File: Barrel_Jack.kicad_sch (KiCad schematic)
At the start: 26 parts, among them J10 Barrel_Jack, J11 Barrel_Jack, J12 Barrel_Jack, J13 Barrel_Jack, J14 Barrel_Jack, J6 Barrel_Jack, J8 Barrel_Jack, J9 Barrel_Jack, U12 PCF8574ATS, U19 34.81-9024, U20 34.81-9024, U21 34.81-9024, U22 34.81-9024, U23 34.81-9024, U24 34.81-9024, U25 34.81-9024, U26 34.81-9024

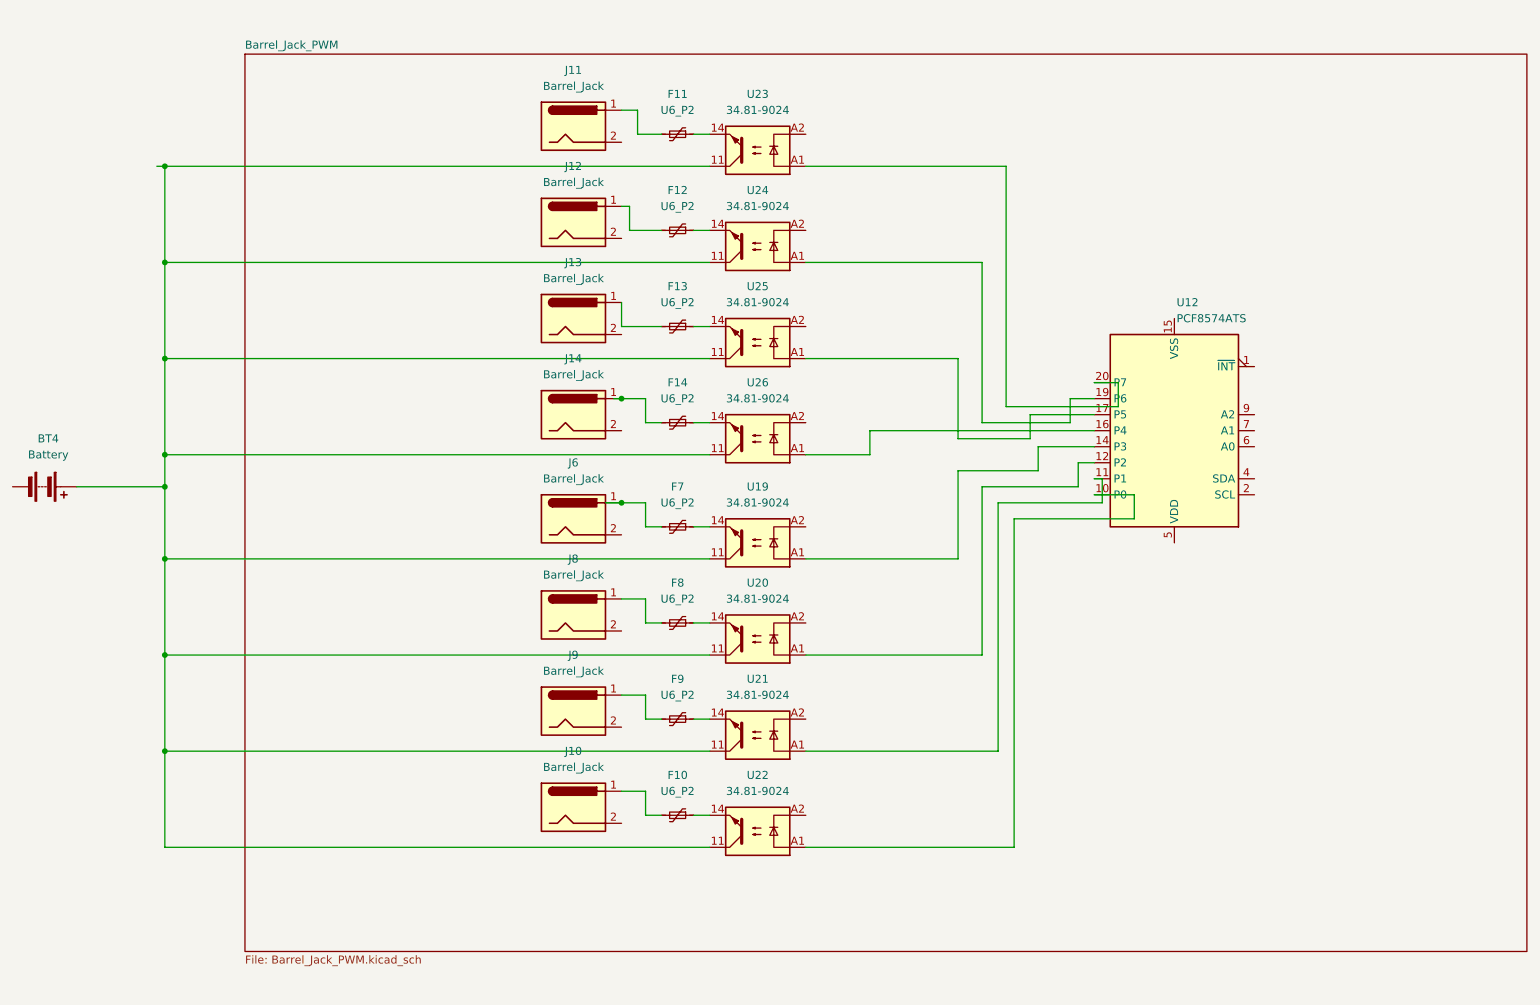
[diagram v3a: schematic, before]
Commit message: placeholders for ethernet and relay inputs
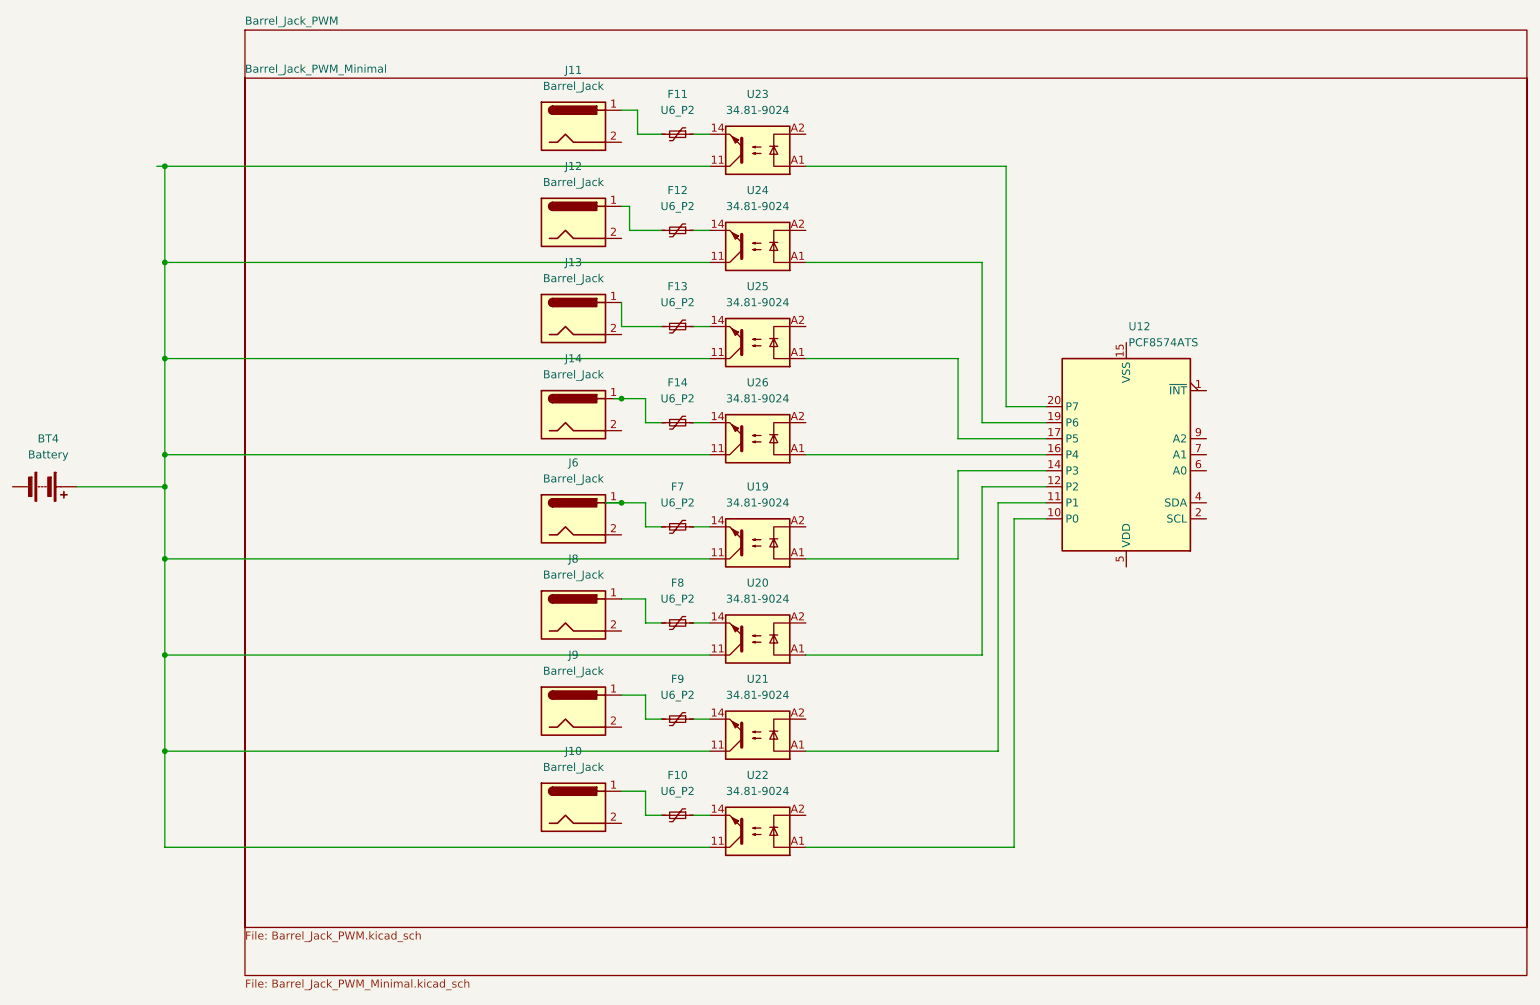
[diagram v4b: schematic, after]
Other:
- added sheet Barrel_Jack_PWM_Minimal (Barrel_Jack_PWM_Minimal.kicad_sch)
- moved on the sheet: U12
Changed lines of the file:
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@@
-    (stroke (width 0) (type default))
-  )
-  (wire (pts (xy 214.63 93.98) (xy 195.58 93.98))
-    (stroke (width 0) (type default))
-  )
-  (wire (pts (xy 205.74 88.9) (xy 205.74 85.09))
-    (stroke (width 0) (type default))
-  )
-  (wire (pts (xy 212.09 76.2) (xy 212.09 72.39))
     (stroke (width 0) (type default))
   )
@@
     (stroke (width 0) (type default))
   )
-  (wire (pts (xy 172.72 83.82) (xy 172.72 80.01))
-    (stroke (width 0) (type default))
-  )
   (wire (pts (xy 139.7 78.74) (xy 137.16 78.74))
     (stroke (width 0) (type default))
@@
     (stroke (width 0) (type default))
   )
-  (wire (pts (xy 209.55 87.63) (xy 208.28 87.63))
-    (stroke (width 0) (type default))
-  )
-  (wire (pts (xy 209.55 91.44) (xy 209.55 87.63))
-    (stroke (width 0) (type default))
-  )
   (wire (pts (xy 134.62 44.45) (xy 133.35 44.45))
     (stroke (width 0) (type default))
@@
     (stroke (width 0) (type default))
   )
-  (wire (pts (xy 204.47 78.74) (xy 190.5 78.74))
+  (wire (pts (xy 190.5 78.74) (xy 200.66 78.74))
     (stroke (width 0) (type default))
   )
@@
     (stroke (width 0) (type default))
   )
-  (wire (pts (xy 190.5 88.9) (xy 205.74 88.9))
-    (stroke (width 0) (type default))
-  )
-  (wire (pts (xy 204.47 74.93) (xy 208.28 74.93))
+  (wire (pts (xy 190.5 88.9) (xy 200.66 88.9))
     (stroke (width 0) (type default))
   )
@@
     (stroke (width 0) (type default))
   )
-  (wire (pts (xy 212.09 72.39) (xy 208.28 72.39))
-    (stroke (width 0) (type default))
-  )
-  (wire (pts (xy 199.39 82.55) (xy 208.28 82.55))
-    (stroke (width 0) (type default))
-  )
-  (wire (pts (xy 198.12 81.28) (xy 186.69 81.28))
+  (wire (pts (xy 194.31 76.2) (xy 200.66 76.2))
+    (stroke (width 0) (type default))
+  )
+  (wire (pts (xy 186.69 81.28) (xy 200.66 81.28))
     (stroke (width 0) (type default))
   )
@@
     (stroke (width 0) (type default))
   )
-  (wire (pts (xy 199.39 86.36) (xy 186.69 86.36))
+  (wire (pts (xy 186.69 86.36) (xy 200.66 86.36))
     (stroke (width 0) (type default))
   )
@@
     (stroke (width 0) (type default))
   )
-  (wire (pts (xy 205.74 85.09) (xy 208.28 85.09))
-    (stroke (width 0) (type default))
-  )
   (wire (pts (xy 137.16 137.16) (xy 137.16 140.97))
     (stroke (width 0) (type default))
@@
     (stroke (width 0) (type default))
   )
+  (wire (pts (xy 200.66 93.98) (xy 195.58 93.98))
+    (stroke (width 0) (type default))
+  )
   (wire (pts (xy 60.96 68.58) (xy 60.96 83.82))
     (stroke (width 0) (type default))
   )
-  (wire (pts (xy 162.56 83.82) (xy 172.72 83.82))
-    (stroke (width 0) (type default))
-  )
   (wire (pts (xy 147.32 68.58) (xy 60.96 68.58))
     (stroke (width 0) (type default))
   )
-  (wire (pts (xy 199.39 86.36) (xy 199.39 82.55))
-    (stroke (width 0) (type default))
-  )
   (wire (pts (xy 144.78 33.02) (xy 147.32 33.02))
     (stroke (width 0) (type default))
@@
     (stroke (width 0) (type default))
   )
-  (wire (pts (xy 198.12 77.47) (xy 208.28 77.47))
-    (stroke (width 0) (type default))
-  )
-  (wire (pts (xy 198.12 81.28) (xy 198.12 77.47))
-    (stroke (width 0) (type default))
-  )
-  (wire (pts (xy 209.55 91.44) (xy 193.04 91.44))
-    (stroke (width 0) (type default))
-  )
-  (wire (pts (xy 212.09 76.2) (xy 194.31 76.2))
+  (wire (pts (xy 193.04 91.44) (xy 200.66 91.44))
     (stroke (width 0) (type default))
   )
@@
     (stroke (width 0) (type default))
   )
-  (wire (pts (xy 214.63 90.17) (xy 208.28 90.17))
-    (stroke (width 0) (type default))
-  )
   (wire (pts (xy 60.96 53.34) (xy 60.96 68.58))
     (stroke (width 0) (type default))
   )
-  (wire (pts (xy 204.47 78.74) (xy 204.47 74.93))
-    (stroke (width 0) (type default))
-  )
   (wire (pts (xy 137.16 140.97) (xy 139.7 140.97))
     (stroke (width 0) (type default))
   )
-  (wire (pts (xy 172.72 80.01) (xy 208.28 80.01))
+  (wire (pts (xy 162.56 83.82) (xy 200.66 83.82))
     (stroke (width 0) (type default))
   )
   (wire (pts (xy 186.69 68.58) (xy 162.56 68.58))
-    (stroke (width 0) (type default))
-  )
-  (wire (pts (xy 214.63 93.98) (xy 214.63 90.17))
     (stroke (width 0) (type default))
   )
@@
     )
   )
-  (symbol (lib_id "Interface_Expansion:PCF8574ATS") (at 220.98 80.01 180) (unit 1)
-    (in_bom yes) (on_board yes) (dnp no) (fields_autoplaced)
-    (property "Reference" "U12" (at 221.3259 59.69 0)
+  (symbol (lib_id "Interface_Expansion:PCF8574ATS") (at 213.36 83.82 180) (unit 1)
+    (in_bom yes) (on_board yes) (dnp no) (fields_autoplaced)
+    (property "Reference" "U12" (at 213.7059 63.5 0)
       (effects (font (size 1.27 1.27)) (justify right))
     )
-    (property "Value" "PCF8574ATS" (at 221.3259 62.23 0)
+    (property "Value" "PCF8574ATS" (at 213.7059 66.04 0)
       (effects (font (size 1.27 1.27)) (justify right))
     )
-    (property "Footprint" "Package_SO:SSOP-20_4.4x6.5mm_P0.65mm" (at 220.98 80.01 0)
-      (effects (font (size 1.27 1.27)) hide)
-    )
-    (property "Datasheet" "http://www.nxp.com/docs/en/data-sheet/PCF8574_PCF8574A.pdf" (at 220.98 80.01 0)
+    (property "Footprint" "Package_SO:SSOP-20_4.4x6.5mm_P0.65mm" (at 213.36 83.82 0)
+      (effects (font (size 1.27 1.27)) hide)
+    )
+    (property "Datasheet" "http://www.nxp.com/docs/en/data-sheet/PCF8574_PCF8574A.pdf" (at 213.36 83.82 0)
       (effects (font (size 1.27 1.27)) hide)
     )
@@
     )
   )
-  (sheet (at 73.66 20.32) (size 203.2 142.24) (fields_autoplaced)
+  (sheet (at 73.66 16.51) (size 203.2 142.24) (fields_autoplaced)
     (stroke (width 0.1524) (type solid))
     (fill (color 0 0 0 0.0000))
-    (property "Sheetname" "Barrel_Jack_PWM" (at 73.66 19.6084 0)
+    (property "Sheetname" "Barrel_Jack_PWM" (at 73.66 15.7984 0)
       (effects (font (size 1.27 1.27)) (justify left bottom))
     )
-    (property "Sheetfile" "Barrel_Jack_PWM.kicad_sch" (at 73.66 163.1446 0)
+    (property "Sheetfile" "Barrel_Jack_PWM.kicad_sch" (at 73.66 159.3346 0)
       (effects (font (size 1.27 1.27)) (justify left top))
     )
@@
       )
     )
+  )
+  (sheet (at 73.66 24.13) (size 203.2 142.24) (fields_autoplaced)
+    (stroke (width 0.1524) (type solid))
+    (fill (color 0 0 0 0.0000))
+    (property "Sheetname" "Barrel_Jack_PWM_Minimal" (at 73.66 23.4184 0)
+      (effects (font (size 1.27 1.27)) (justify left bottom))
+    )
+    (property "Sheetfile" "Barrel_Jack_PWM_Minimal.kicad_sch" (at 73.66 166.9546 0)
+      (effects (font (size 1.27 1.27)) (justify left top))
+    )
+    (instances
+      (project "esp"
+        (path "/dab6683c-420f-459a-bf9c-0c28b4b081e3/d534b787-d3bc-419e-b481-23d8b9503201" (page "7"))
+      )
+    )

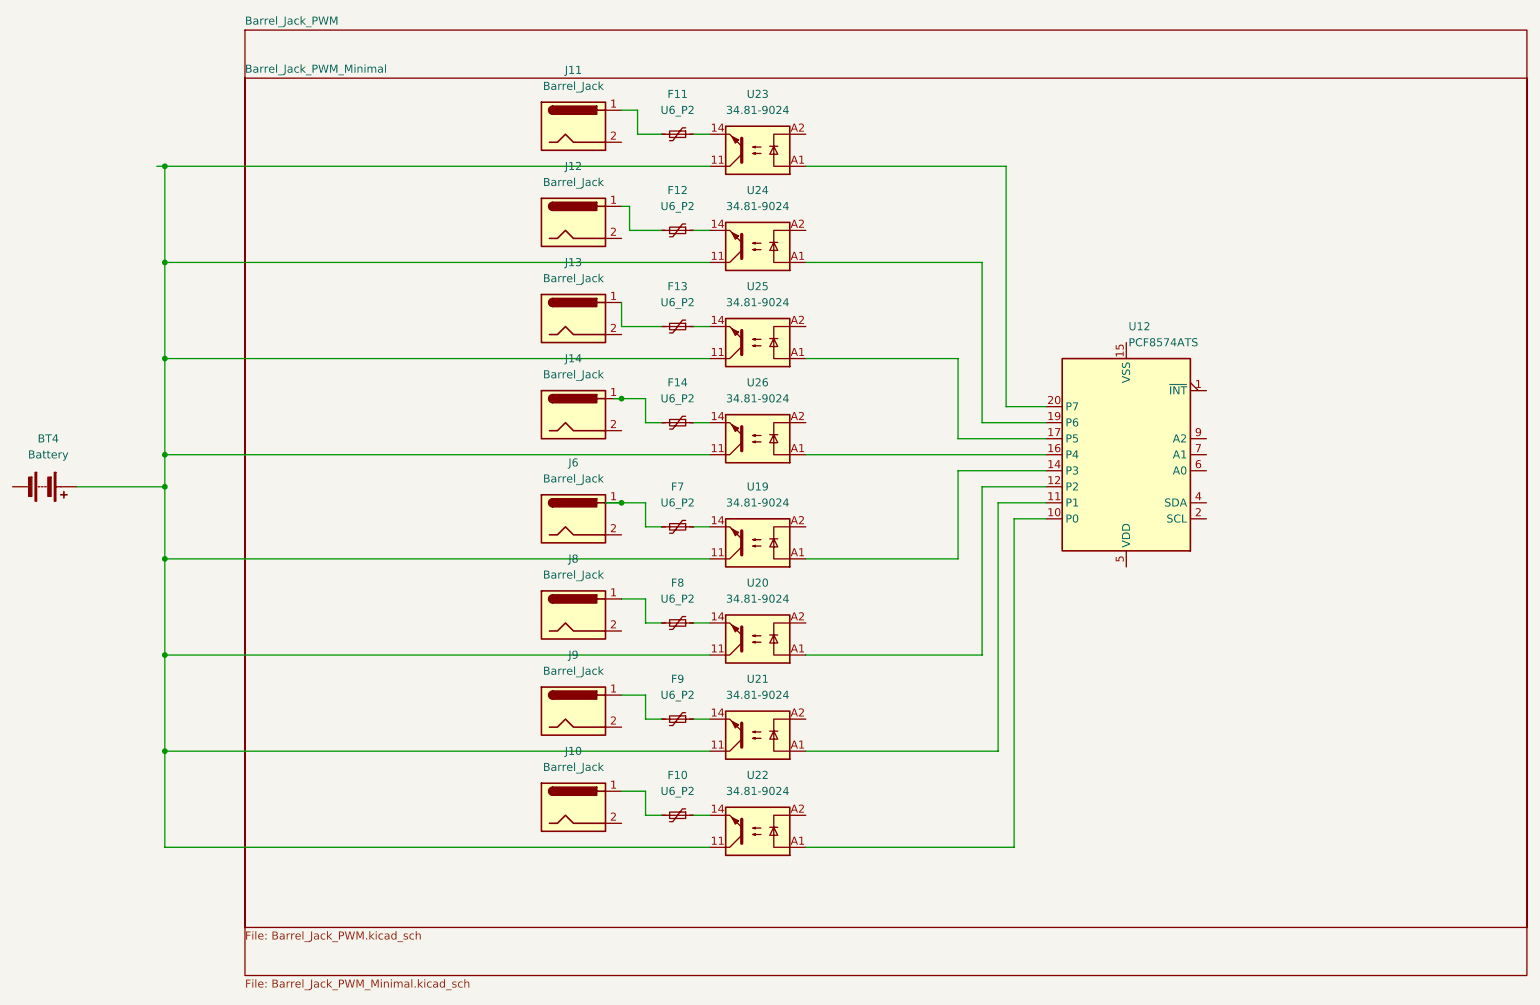
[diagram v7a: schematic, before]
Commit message: add level converter to be compatible with high volt relay
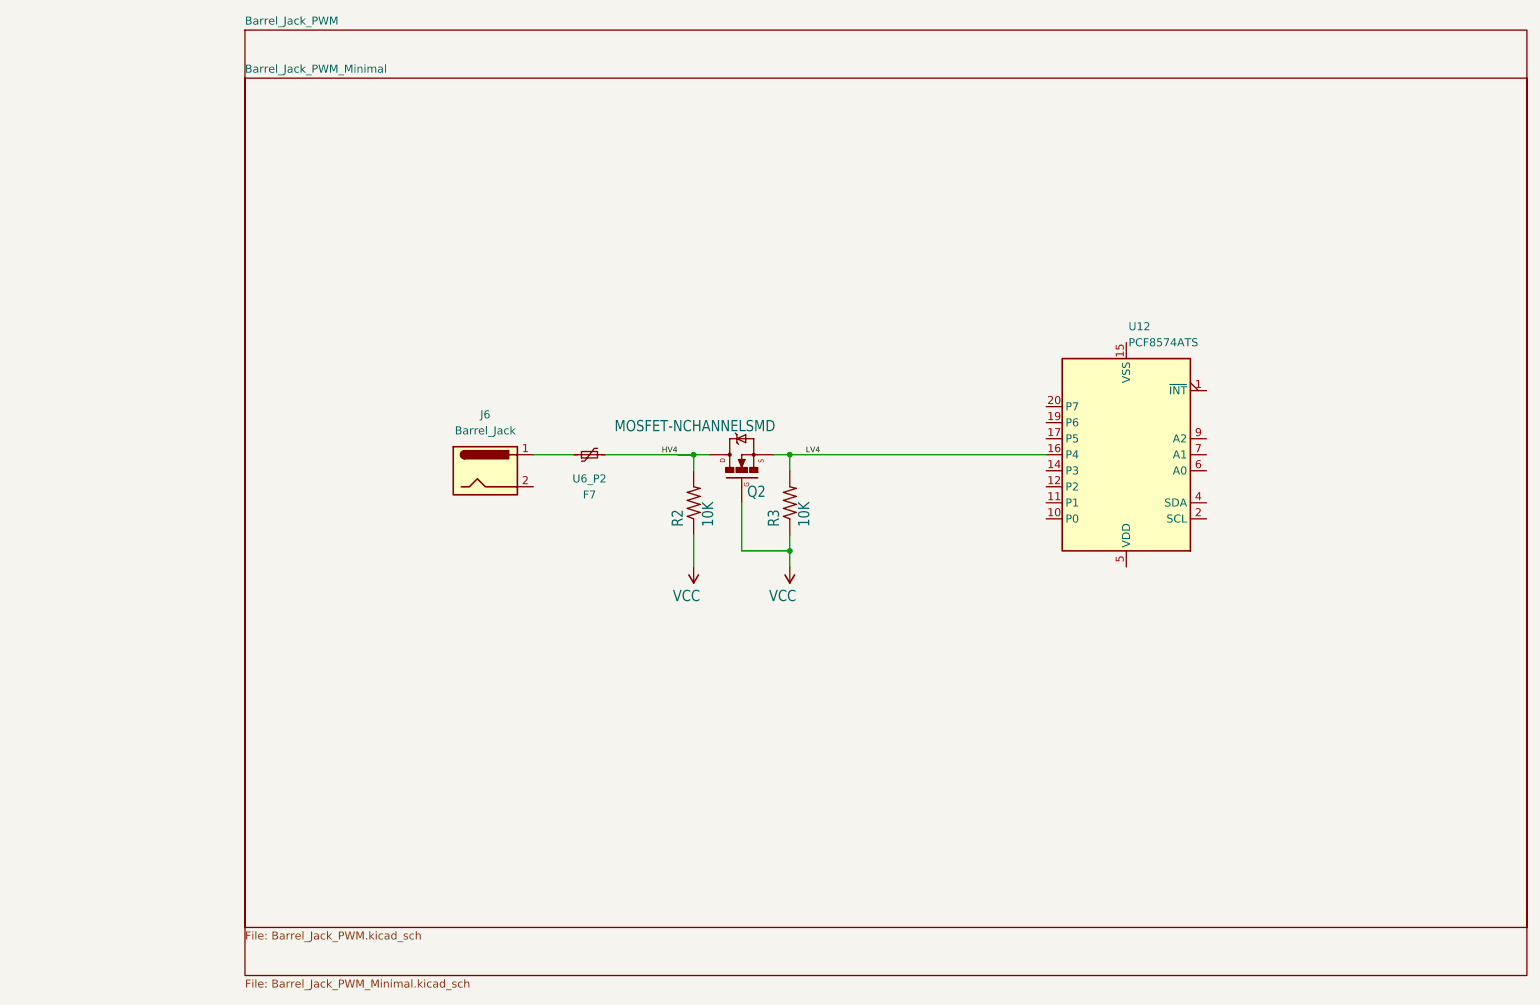
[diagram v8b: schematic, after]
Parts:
- removed BT4: Battery, symbol Device:Battery
- removed F10, F11, F12, F13, F14, F8, F9: U6_P2, symbol Device:Polyfuse_Small
- removed J10, J11, J12, J13, J14, J8, J9: Barrel_Jack, symbol Connector:Barrel_Jack
- removed U19, U20, U21, U22, U23, U24, U25, U26: 34.81-9024, OptoDevice:Finder_34.81, symbol Relay_SolidState:34.81-9024
- added Q2: MOSFET-NCHANNELSMD, Logic_Level_Bidirectional:SOT23-3, symbol Logic_Level_Bidirectional-eagle-import:MOSFET-NCHANNELSMD
- added R2, R3: 10K, Logic_Level_Bidirectional:0603-RES, symbol Logic_Level_Bidirectional-eagle-import:RESISTOR0603-RES
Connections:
- net LV4: now reaches U12.16 (P4)
- net LV4: now also Q2.2 (S), R3.2
- net at J6.1: now also F7.1; no longer F7.2
- new net HV4: F7.2, Q2.3 (D), R2.2
- new net VCC: Q2.1 (G), R2.1, R3.1
